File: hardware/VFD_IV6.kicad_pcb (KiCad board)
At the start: 2 copper layers, 125.6 x 80.8 mm, 107 parts, among them J1 Conn_01x09, Q2 BC817, U1 4511, U10 TBD62783A, U11 4511, U12 TBD62783A, U13 4017, U2 TBD62783A, U3 4511, U4 TBD62783A, U5 4511, U6 TBD62783A, U7 4511, U8 TBD62783A, U9 4511

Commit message: New board draft
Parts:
- removed R11, R12, R13, R14, R15, R16, R17, R2, R20, R21, R22, R23, R24, R25, R26, R29, R3, R30, R31, R32, R33, R34, R35, R38, R39, R4, R40, R41, R42, R43, R44, R47, R48, R49, R5, R50, R51, R52, R53, R6, R7, R8: 47k, Resistor_SMD:R_0603_1608Metric
- removed the R60 at (185.7, 147.5)
- removed the R60 at (149.1, 147.5)
- removed the R60 at (222.8, 128.3)
- removed the R60 at (124.7, 86.6)
- removed the R60 at (157.0, 84.1)
- removed the R60 at (114.8, 116.1)
- removed the R60 at (122.4, 86.6)
- removed the R60 at (191.3, 117.1)
- removed the R60 at (150.9, 111.2)
- removed the R60 at (188.0, 109.0)
- removed the R60 at (185.4, 109.0)
- removed the R60 at (186.9, 119.9)
- removed the R60 at (169.9, 119.9)
- removed the R60 at (150.1, 119.9)
- removed U13: 4017, Package_DIP:DIP-16_W8.89mm_SMDSocket_LongPads
- removed VFD_PWR1: ~, Library:VFD_PowerSupply
- added BT1: CR1220, Library:RSPRO1220, B.Cu at (134.0, 47.5)
- added BZ1: Buzzer, Buzzer_Beeper:Buzzer_12x9.5RM7.6, B.Cu at (153.5, 45.3)
- added C10: 100n, Capacitor_SMD:C_0603_1608Metric, B.Cu at (158.4, 85.1)
- added C11: 100n, Capacitor_SMD:C_0603_1608Metric, B.Cu at (184.2, 43.1)
- added C12: 100n, Capacitor_SMD:C_0603_1608Metric, B.Cu at (184.2, 45.6)
- added C13: 100n, Capacitor_SMD:C_0603_1608Metric, B.Cu at (184.2, 48.1)
- added C14: 100n, Capacitor_SMD:C_0603_1608Metric, B.Cu at (184.2, 50.7)
- added C15: 100n, Capacitor_SMD:C_0603_1608Metric, B.Cu at (184.2, 53.2)
- added C16: 22p, Capacitor_SMD:C_0603_1608Metric, B.Cu at (184.2, 55.7)
- added C17: 22p, Capacitor_SMD:C_0603_1608Metric, B.Cu at (188.2, 35.6)
- added C18: 10n, Capacitor_SMD:C_0603_1608Metric, F.Cu at (151.4, 80.9)
- added C19: 2u2, Capacitor_SMD:C_0805_2012Metric, F.Cu at (149.4, 80.6)
- added C20: 1u, Capacitor_SMD:C_0805_2012Metric, F.Cu at (150.4, 88.0)
- added C21: 100n, Capacitor_SMD:C_0603_1608Metric, F.Cu at (148.0, 94.2)
- added C22: 3n9, Capacitor_SMD:C_0603_1608Metric, F.Cu at (154.0, 93.3)
- added C23: 10u 25v, Capacitor_SMD:C_0805_2012Metric, F.Cu at (150.6, 104.3)
- added C24: 10u 25v, Capacitor_SMD:C_0805_2012Metric, F.Cu at (150.6, 106.4)
- added C25: 10n, Capacitor_SMD:C_0603_1608Metric, F.Cu at (148.0, 104.8)
- added C26: 22u 6,3v, Capacitor_SMD:C_1210_3225Metric, F.Cu at (155.4, 99.6)
- added C27: 82p, Capacitor_SMD:C_0603_1608Metric, F.Cu at (148.5, 64.9)
- added C28: 10u, Capacitor_SMD:C_0805_2012Metric, F.Cu at (152.3, 69.3)
- added C29: 2u2 50v, Capacitor_SMD:C_1210_3225Metric, F.Cu at (147.7, 60.9)
- added C30: 100n, Capacitor_SMD:C_0805_2012Metric, B.Cu at (70.6, 74.9)
- added C31: 220u, Capacitor_Tantalum_SMD:CP_EIA-7360-38_Kemet-E, B.Cu at (152.8, 87.6)
- added C9: 100n, Capacitor_SMD:C_0603_1608Metric, B.Cu at (158.4, 75.3)
- added D5: MBR0530, Diode_SMD:D_SOD-123, F.Cu at (152.5, 61.1)
- added H1: MountingHole, MountingHole:MountingHole_2.7mm_M2.5_DIN965_Pad, F.Cu at (62.1, 106.8)
- added H2: MountingHole, MountingHole:MountingHole_2.7mm_M2.5_DIN965_Pad, F.Cu at (62.1, 60.3)
- added H3: MountingHole, MountingHole:MountingHole_2.7mm_M2.5_DIN965_Pad, F.Cu at (164.8, 60.2)
- added H4: MountingHole, MountingHole:MountingHole_2.7mm_M2.5_DIN965_Pad, F.Cu at (165.1, 106.9)
- added J2: USB_C, Connector_USB:USB_C_Receptacle_HRO_TYPE-C-31-M-17, F.Cu at (165.9, 94.4)
- added J3: Conn_01x10, Connector_PinHeader_2.54mm:PinHeader_1x10_P2.54mm_Vertical, B.Cu at (104.3, 27.8)
- added J4: Conn_01x06, Connector_PinHeader_2.54mm:PinHeader_1x08_P2.54mm_Vertical, B.Cu at (76.8, 27.7)
- added L1: 2,2uH, Inductor_SMD:L_APV_APH0650, F.Cu at (156.9, 105.3)
- added L2: 10uH, Inductor_SMD:L_APV_APH0650, F.Cu at (157.9, 66.3)
- added Q3: BC817, Package_TO_SOT_SMD:SOT-23, B.Cu at (192.8, 64.8)
- added R60: 10k, Resistor_SMD:R_0603_1608Metric, B.Cu at (161.9, 77.0)
- added R61: 10k, Resistor_SMD:R_0603_1608Metric, B.Cu at (158.4, 77.0)
- added R62: 10k, Resistor_SMD:R_0603_1608Metric, B.Cu at (161.6, 85.1)
- added R63: 10k, Resistor_SMD:R_0603_1608Metric, B.Cu at (196.2, 40.6)
- added R64: 10k, Resistor_SMD:R_0603_1608Metric, B.Cu at (196.2, 43.1)
- added R65: 10k, Resistor_SMD:R_0603_1608Metric, B.Cu at (196.2, 45.6)
- added R66: 1M, Resistor_SMD:R_0603_1608Metric, B.Cu at (196.2, 48.1)
- added R67: 5k1, Resistor_SMD:R_0603_1608Metric, F.Cu at (159.0, 96.3)
- added R68: 5k1, Resistor_SMD:R_0603_1608Metric, F.Cu at (160.5, 96.3)
- added R69: 10k, Resistor_SMD:R_0603_1608Metric, F.Cu at (149.6, 94.2)
- added R70: 6k8, Resistor_SMD:R_0603_1608Metric, F.Cu at (151.1, 94.2)
- added R71: 1k8, Resistor_SMD:R_0603_1608Metric, F.Cu at (153.4, 94.9)
- added R72: 10k, Resistor_SMD:R_0603_1608Metric, F.Cu at (154.0, 96.5)
- added R73: 47k, Resistor_SMD:R_0603_1608Metric, F.Cu at (152.3, 67.5)
- added R74: 330k, Resistor_SMD:R_0603_1608Metric, F.Cu at (148.5, 63.4)
- added R75: 13,3k, Resistor_SMD:R_0603_1608Metric, F.Cu at (148.5, 66.4)
- added R76: 10k, Resistor_SMD:R_0603_1608Metric, B.Cu at (200.2, 50.7)
- added RESET1: SW_SPST, Button_Switch_SMD:SW_SPST_CK_RS282G05A3, B.Cu at (135.9, 36.1)
- added SW1: RotaryEncoder_Switch_MP, Rotary_Encoder:RotaryEncoder_Alps_EC12E-Switch_Vertical_H20mm, F.Cu at (162.6, 73.0)
- added U14: 74HC04, Package_SO:SOIC-14_3.9x8.7mm_P1.27mm, B.Cu at (65.9, 69.3)
- added U15: STM32F103C8T6, Package_QFP:LQFP-48_7x7mm_P0.5mm, B.Cu at (91.8, 41.5)
- added U16: LP2985-3.3, Package_TO_SOT_SMD:SOT-23-5, F.Cu at (150.4, 84.6)
- added U17: DS1302Z+, Package_SO:SOIC-8_5.3x5.3mm_P1.27mm, B.Cu at (109.3, 49.3)
- added U18: MP2307, Package_SO:SOIC-8_3.9x4.9mm_P1.27mm, F.Cu at (149.9, 99.5)
- added U19: LM2733XMF, Package_TO_SOT_SMD:SOT-23-5, F.Cu at (152.3, 64.6)
- added U20: 4017, Package_SO:SOIC-16_3.9x9.9mm_P1.27mm, B.Cu at (75.0, 68.7)
- added Y1: 8MHz, Crystal:Crystal_SMD_HC49-SD, B.Cu at (153.2, 39.2)
- added Y2: 32,768kHz, Crystal:Crystal_AT310_D3.0mm_L10.0mm_Horizontal, B.Cu at (118.4, 39.0)
- C1: value 100u -> 100n; footprint Capacitor_Tantalum_SMD:CP_EIA-7343-31_Kemet-D -> Capacitor_SMD:C_0603_1608Metric
- D1, D2, D3, D4: footprint LED_THT:LED_D3.0mm_Clear -> LED_SMD:LED_0603_1608Metric
- J1: value Conn_01x09 -> SWD; footprint Connector_PinHeader_2.54mm:PinHeader_1x09_P2.54mm_Vertical -> Connector_PinHeader_2.54mm:PinHeader_1x04_P2.54mm_Vertical; moved to B.Cu
- R55, R56, R57, R58: value 470 -> 4k7
- R59: value 25k -> 18k
- VFD1, VFD2, VFD3, VFD4, VFD5, VFD6: footprint Library:IV-6 -> Library:IV-6_Horizontal
- moved C2 147.0 mm to (62.7, 82.7)
- moved U2 146.9 mm to (71.2, 90.7)
- moved U1 146.8 mm to (69.3, 80.5)
- moved R9 146.7 mm to (63.0, 79.5)
- moved VFD1 146.6 mm to (71.3, 103.5)
- moved R1 146.4 mm to (73.7, 104.9), turned to 180 degrees
- moved R18 118.5 mm to (87.0, 104.9), turned to 180 degrees
- moved C3 118.3 mm to (75.9, 82.7)
- moved VFD2 118.3 mm to (84.5, 103.5)
- moved U4 118.1 mm to (84.5, 90.7)
- moved U3 118.0 mm to (82.5, 80.5)
- moved R10 117.8 mm to (76.2, 79.5)
- moved R57 94.4 mm to (192.2, 48.1), turned to 180 degrees
- moved J1 94.3 mm to (128.4, 22.6), turned to 180 degrees
- moved R58 92.8 mm to (192.2, 50.7), turned to 180 degrees
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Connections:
- C1 pad 1: +5V -> /ENCA
- J1 pad 2: /COLON -> /SWCLK
- J1 pad 3: /DCLOCK -> /SWDIO
- J1 pad 4: /DD -> +3V3
- VFD1 pad 1: Net-(VFD1-b) -> Net-(U2-O4)
- VFD1 pad 10: Net-(VFD1-c) -> Net-(U2-O5)
- VFD1 pad 2: Net-(VFD1-a) -> Net-(U2-O3)
- VFD1 pad 3: Net-(VFD1-g) -> Net-(U2-O2)
- VFD1 pad 4: Net-(VFD1-f) -> Net-(U2-O1)
- VFD1 pad 5: Net-(VFD1-e) -> Net-(U2-O7)
- VFD1 pad 6: Net-(VFD1-d) -> Net-(U2-O6)
- VFD2 pad 1: Net-(VFD2-b) -> Net-(U4-O4)
- VFD2 pad 10: Net-(VFD2-c) -> Net-(U4-O5)
- VFD2 pad 2: Net-(VFD2-a) -> Net-(U4-O3)
- VFD2 pad 3: Net-(VFD2-g) -> Net-(U4-O2)
- VFD2 pad 4: Net-(VFD2-f) -> Net-(U4-O1)
- VFD2 pad 5: Net-(VFD2-e) -> Net-(U4-O7)
- VFD2 pad 6: Net-(VFD2-d) -> Net-(U4-O6)
- VFD3 pad 1: Net-(VFD3-b) -> Net-(U6-O4)
- VFD3 pad 10: Net-(VFD3-c) -> Net-(U6-O5)
- VFD3 pad 2: Net-(VFD3-a) -> Net-(U6-O3)
- VFD3 pad 3: Net-(VFD3-g) -> Net-(U6-O2)
- VFD3 pad 4: Net-(VFD3-f) -> Net-(U6-O1)
- VFD3 pad 5: Net-(VFD3-e) -> Net-(U6-O7)
- VFD3 pad 6: Net-(VFD3-d) -> Net-(U6-O6)
- VFD4 pad 1: Net-(VFD4-b) -> Net-(U8-O4)
- VFD4 pad 10: Net-(VFD4-c) -> Net-(U8-O5)
- VFD4 pad 2: Net-(VFD4-a) -> Net-(U8-O3)
- VFD4 pad 3: Net-(VFD4-g) -> Net-(U8-O2)
- VFD4 pad 4: Net-(VFD4-f) -> Net-(U8-O1)
- VFD4 pad 5: Net-(VFD4-e) -> Net-(U8-O7)
- VFD4 pad 6: Net-(VFD4-d) -> Net-(U8-O6)
- VFD5 pad 1: Net-(VFD5-b) -> Net-(U10-O4)
- VFD5 pad 10: Net-(VFD5-c) -> Net-(U10-O5)
- VFD5 pad 2: Net-(VFD5-a) -> Net-(U10-O3)
- VFD5 pad 3: Net-(VFD5-g) -> Net-(U10-O2)
- VFD5 pad 4: Net-(VFD5-f) -> Net-(U10-O1)
- VFD5 pad 5: Net-(VFD5-e) -> Net-(U10-O7)
- VFD5 pad 6: Net-(VFD5-d) -> Net-(U10-O6)
- VFD6 pad 1: Net-(VFD6-b) -> Net-(U12-O4)
- VFD6 pad 10: Net-(VFD6-c) -> Net-(U12-O5)
- VFD6 pad 2: Net-(VFD6-a) -> Net-(U12-O3)
- VFD6 pad 3: Net-(VFD6-g) -> Net-(U12-O2)
- VFD6 pad 4: Net-(VFD6-f) -> Net-(U12-O1)
- VFD6 pad 5: Net-(VFD6-e) -> Net-(U12-O7)
- VFD6 pad 6: Net-(VFD6-d) -> Net-(U12-O6)
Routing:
- net +36V: track 242.0 -> 0.00 mm
- net +5V: track 295.2 -> 71.4 mm, vias 0 -> 5
- net /DIMPWM: track 170.0 -> 0.00 mm, vias 6 -> 0
- net /DD: track 160.2 -> 0.00 mm, vias 6 -> 0
- net /DC: track 148.7 -> 0.00 mm, vias 6 -> 0
- net /DB: track 141.7 -> 0.00 mm, vias 6 -> 0
- net /DA: track 128.7 -> 0.00 mm, vias 6 -> 0
- net Net-(U3-~{EL}): track 114.3 -> 0.00 mm, vias 2 -> 0
- net Net-(U1-~{EL}): track 100.3 -> 11.8 mm
- net Net-(U5-~{EL}): track 68.7 -> 0.00 mm, vias 2 -> 0
- net Net-(D1-K): track 64.9 -> 0.00 mm
- net /DCLOCK: track 62.7 -> 0.00 mm
- net Net-(U7-~{EL}): track 32.7 -> 0.00 mm
- net Net-(U11-~{EL}): track 28.6 -> 0.00 mm
- net +1V2: track 164.1 -> 138.0 mm, vias 0 -> 2
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- removed copper zone on B.Cu, net GND
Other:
- board size 125.6 x 80.8 mm -> 110 x 53.6 mm
- board text removed: "VFD CLOCK"
- board text removed: "prototype"

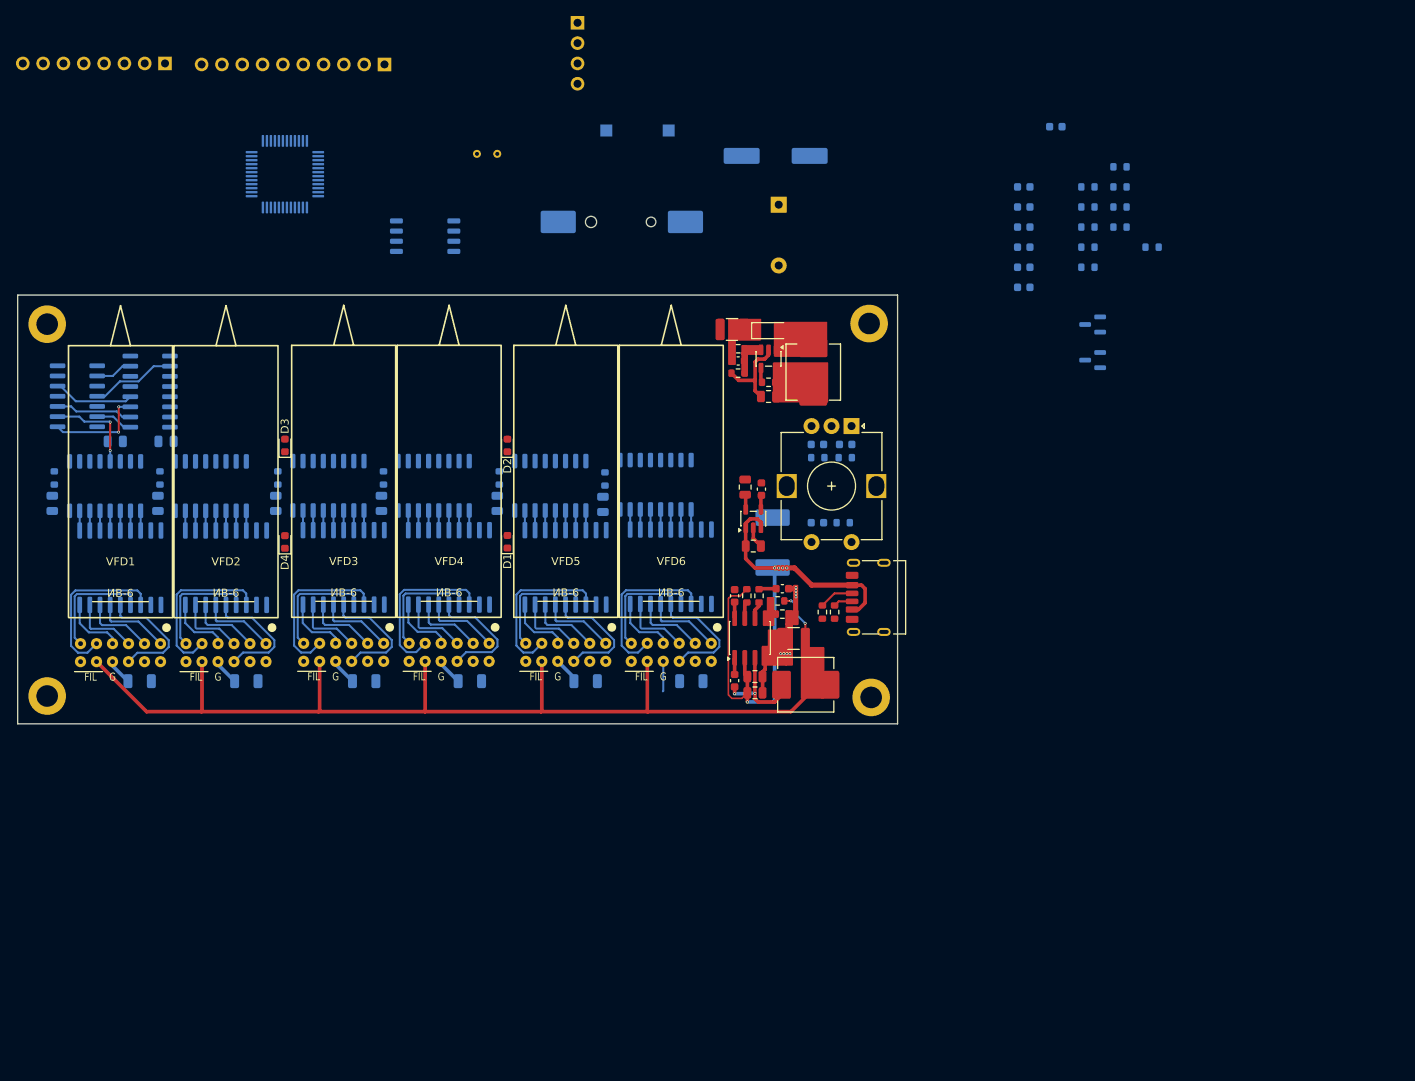
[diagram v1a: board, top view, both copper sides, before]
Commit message: New 4-layer board layout
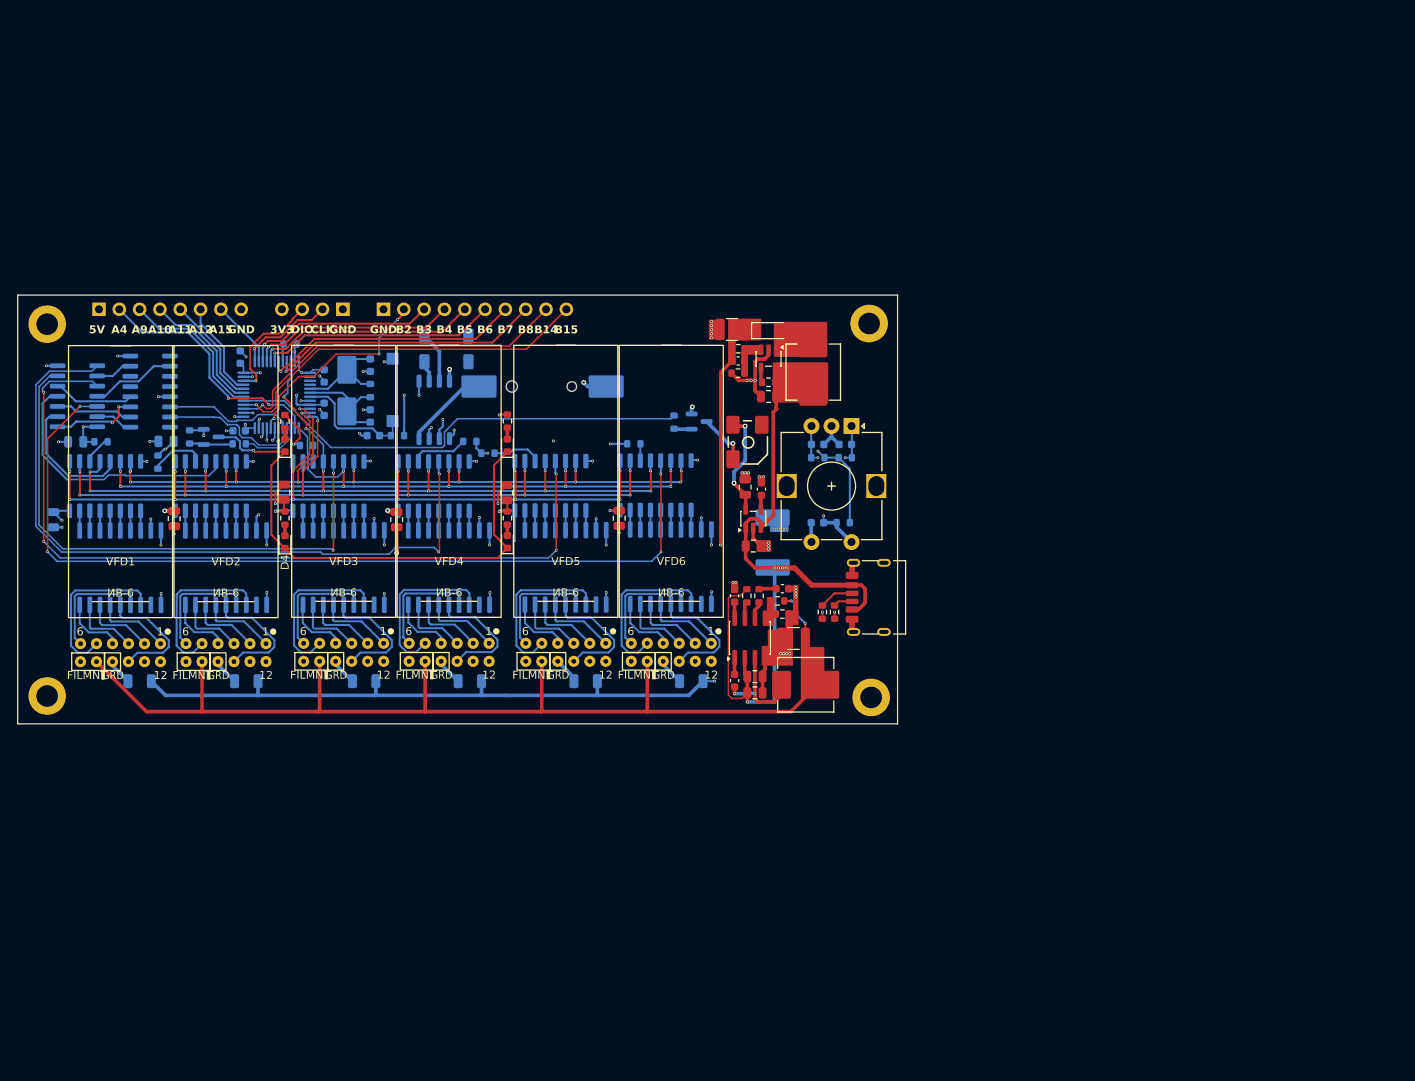
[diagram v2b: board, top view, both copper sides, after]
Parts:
- BZ1: value Buzzer -> ~; footprint Buzzer_Beeper:Buzzer_12x9.5RM7.6 -> Library:HCT5020; moved to F.Cu
- C3, C4, C5, C6, C7, R55, R56, R57, R58: moved to F.Cu
- Y1: footprint Crystal:Crystal_SMD_HC49-SD -> Crystal:Crystal_SMD_5032-2Pin_5.0x3.2mm_HandSoldering
- Y2: value 32,768kHz -> 32.768 KHz; footprint Crystal:Crystal_AT310_D3.0mm_L10.0mm_Horizontal -> Crystal:Crystal_SMD_SeikoEpson_MC306-4Pin_8.0x3.2mm
- moved R76 122.6 mm to (79.9, 74.4), turned to -90 degrees
- moved Q2 111.1 mm to (82.6, 74.4), turned to 0 degrees
- moved R59 108.4 mm to (86.1, 75.2)
- moved R58 105.9 mm to (91.8, 84.5), turned to -90 degrees
- moved R65 105.1 mm to (92.5, 62.7), turned to 0 degrees
- moved R57 103.3 mm to (91.8, 72.5), turned to -90 degrees
- moved C15 100.2 mm to (86.1, 73.6)
- moved C13 99.3 mm to (86.2, 64.4), turned to 90 degrees
- moved R66 95.9 mm to (102.5, 68.6), turned to -90 degrees
- moved R64 95.5 mm to (105.9, 74.2)
- moved C17 90.7 mm to (102.5, 65.4), turned to 90 degrees
- moved C12 90.0 mm to (96.7, 66.8), turned to -90 degrees
- moved C14 89.8 mm to (96.7, 70.9), turned to -90 degrees
- moved C11 87.0 mm to (102.9, 74.2)
- moved R55 83.5 mm to (119.6, 84.5), turned to -90 degrees
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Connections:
- BZ1 pad 1: +5V -> +3V3
- H1 pad 1: (no net) -> GND
- H2 pad 1: (no net) -> GND
- H3 pad 1: (no net) -> GND
- H4 pad 1: (no net) -> GND
- J4 pad 2: /PA7 -> /PA4
- U15 pad 14: /DCLOCK -> /PA4
- U15 pad 17: /PA7 -> /DCLOCK
- Y2 pad 1: Net-(U17-X1) -> Net-(U17-X2)
- Y2 pad 2: Net-(U17-X2) -> unconnected-(Y2-G-Pad2)
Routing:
- net +5V: track 71.4 -> 315.4 mm, vias 5 -> 17
- net +36V: track 0.00 -> 201.1 mm, vias 0 -> 8
- net +3V3: track 1.88 -> 142.6 mm, vias 0 -> 9
- net Net-(U11-~{EL}): track 0.00 -> 111.2 mm, vias 0 -> 4
- net /DIMPWM: track 0.00 -> 108.6 mm, vias 0 -> 14
- net /DB: track 0.00 -> 107.2 mm, vias 0 -> 13
- net Net-(U9-~{EL}): track 0.00 -> 103.2 mm, vias 0 -> 4
- net /DC: track 0.00 -> 102.6 mm, vias 0 -> 13
- net /DD: track 0.00 -> 98.5 mm, vias 0 -> 12
- net /DA: track 0.00 -> 96.9 mm, vias 0 -> 14
- net /ENCA: track 0.00 -> 92.7 mm, vias 0 -> 2
- net Net-(U7-~{EL}): track 0.00 -> 90.1 mm, vias 0 -> 2
- net /ENCBUT: track 0.00 -> 88.9 mm, vias 0 -> 2
- net /ENCB: track 0.00 -> 88.8 mm, vias 0 -> 2
- net GND: track 17.9 -> 94.2 mm, vias 8 -> 78
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- added copper zone on In2.Cu, net GND
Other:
- copper layers 2 -> 4
- board text added: "3V3"
- board text added: "5V"
- board text added: "A10"
- board text added: "A11"
- board text added: "A12"
- board text added: "A15"
- board text added: "A4"
- board text added: "A9"
- board text added: "B14"
- board text added: "B15"
- board text added: "B2"
- board text added: "B3"
- board text added: "B4"
- board text added: "B5"
- board text added: "B6"
- board text added: "B7"
- board text added: "B8"
- board text added: "CLK"
- board text added: "DIO"
- board text added: "GND"

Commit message: Updated kicad project + iBOM
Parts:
- added TP1: 3V3, TestPoint:TestPoint_Pad_1.0x1.0mm, B.Cu at (146.1, 80.2)
- added TP2: 5V, TestPoint:TestPoint_Pad_1.0x1.0mm, F.Cu at (159.4, 91.5)
- added TP3: 1V2, TestPoint:TestPoint_Pad_1.0x1.0mm, F.Cu at (145.4, 107.4)
- added TP4: 30v, TestPoint:TestPoint_Pad_1.0x1.0mm, F.Cu at (135.1, 107.4)
- added TP4: 30v, TestPoint:TestPoint_Pad_1.0x1.0mm, F.Cu at (142.4, 107.5)
- added TP4: 30v, TestPoint:TestPoint_Pad_1.0x1.0mm, B.Cu at (80.1, 69.3)
- moved H4 0.24 mm to (164.9, 106.8)
- moved H2 0.08 mm to (62.1, 60.2)
- moved H3 0.05 mm to (164.9, 60.2)
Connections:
- H1 pad 1: GND -> (no net)
- H2 pad 1: GND -> (no net)
- H3 pad 1: GND -> (no net)
- H4 pad 1: GND -> (no net)
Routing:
- net GND: track 94.2 -> 99.2 mm, vias 78 -> 77
- net +36V: track 201.1 -> 205.4 mm
- net +3V3: track 142.6 -> 145.0 mm
- net /DCLOCK: track 16.4 -> 17.7 mm
- net +5V: track 315.4 -> 316.7 mm
- net +1V2: track 138.0 -> 139.2 mm
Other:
- board size 110 x 53.6 mm -> 110 x 54 mm
- board text added: "1V2"
- board text added: "36V"
- board text added: "CR1220"
- board text added: "DCLK"
- board text added: "ИВ-6 VFD Digital Clock"

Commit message: Updated the board
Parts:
- added REF**: ESD-Logo_6.6x6mm_SilkScreen, Symbol:ESD-Logo_6.6x6mm_SilkScreen, F.Cu at (74.1, 107.1)
- added REF**: OSHW-Symbol_6.7x6mm_SilkScreen, Symbol:OSHW-Symbol_6.7x6mm_SilkScreen, B.Cu at (142.5, 64.7)
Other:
- board text added: "FRAGILE"
- board text added: "HANDLE WITH CAUTION"
- board text added: "Rev. 1"

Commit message: Updated board project and gerber files
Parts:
- moved R9 0.05 mm to (68.9, 75.0)
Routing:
- net +36V: track 205.4 -> 208.8 mm
- net /ENCA: track 92.7 -> 94.4 mm
- net GND: track 99.2 -> 100.1 mm, vias 77 -> 74
- net /ENCB: track 88.8 -> 89.6 mm
- net /DA: track 96.9 -> 97.5 mm
- net /SWDIO: track 14.6 -> 15.2 mm
- net Net-(U10-O7): track 20.9 -> 21.5 mm
- net Net-(U12-O7): track 20.9 -> 21.4 mm
- net /RTC_DAT: track 26.6 -> 27.1 mm

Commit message: Updated schematic and board
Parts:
- added C19: 100n, Capacitor_SMD:C_0603_1608Metric, B.Cu at (137.4, 64.2)
- added F1: 0,75A 6V, Fuse:Fuse_1210_3225Metric, F.Cu at (158.5, 90.9)
- added J3: Power, Connector_JST:JST_XH_B2B-XH-A_1x02_P2.50mm_Vertical, B.Cu at (163.7, 66.0)
- added R21: 10k, Resistor_SMD:R_0603_1608Metric, B.Cu at (137.4, 65.8)
- added R24: 0, Resistor_SMD:R_0603_1608Metric, B.Cu at (133.5, 64.2)
- added SW2: MODE, Button_Switch_THT:SW_Tactile_SPST_Angled_PTS645Vx39-2LFS, B.Cu at (138.3, 58.4)
- moved TP1 11.5 mm to (147.9, 91.3)
- moved REF** 2.54 mm to (145.0, 64.7)
- renumbered C20 to C1, C19 to C10, C22 to C11, C25 to C12, C27 to C13, C29 to C14, C26 to C15, C11 to C16, C16 to C18, C1 to C2, C31 to C20, C12 to C21, C13 to C22, C30 to C23, C14 to C24, C15 to C25, C8 to C26, C2 to C27, C3 to C28, C4 to C29, C9 to C3, C5 to C30, C6 to C31, C7 to C32, C24 to C4, C23 to C5, C18 to C6, C21 to C7, C10 to C8, C28 to C9, D5 to D1, D1 to D2, D2 to D3, D3 to D4, D4 to D5, J2 to J1, J1 to J2, J3 to J4, J4 to J5, L2 to L1, L1 to L2, Q3 to Q1, R61 to R1, R72 to R10, R71 to R11, R55 to R12, R59 to R13, R76 to R14, R56 to R15, R57 to R16, R58 to R17, R64 to R18, R65 to R19, R60 to R2, R66 to R20, R67 to R22, R68 to R23, R9 to R25, R10 to R26, R19 to R27, R37 to R29, R62 to R3, R46 to R30, R1 to R31, R18 to R32, R27 to R33, R36 to R34, R45 to R35, R54 to R36, R69 to R4, R73 to R5, R70 to R6, R75 to R7, R63 to R8, R74 to R9, TP2 to TP1, TP1 to TP2, TP4 to TP3, TP3 to TP4, U16 to U1, U5 to U10, U7 to U11, U9 to U12, U11 to U13, U2 to U14, U4 to U15, U6 to U16, U8 to U17, U10 to U18, U12 to U19, U18 to U2, U19 to U3, U17 to U4, U15 to U5, U14 to U6, U20 to U7, U1 to U8, U3 to U9, Y2 to Y1, Y1 to Y2
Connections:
- J1 pad A9: +5V -> Net-(F1-Pad2)
- J1 pad B9: +5V -> Net-(F1-Pad2)
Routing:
- net +5V: track 316.8 -> 337.9 mm
- net Net-(SW2-B): track 0.00 -> 9.83 mm
- net Net-(F1-Pad2): track 0.00 -> 9.21 mm
- net /PB15: track 47.3 -> 55.5 mm
- net GND: track 100.1 -> 106.1 mm
- net +3V3: track 144.9 -> 148.8 mm, vias 9 -> 10
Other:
- board text added: "- POWER +"
- board text added: "MODE"
- board text added: "RST"
